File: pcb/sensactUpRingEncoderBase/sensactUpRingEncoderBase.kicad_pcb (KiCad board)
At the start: 2 copper layers, 70 x 70 mm, 59 parts, among them J3 BaseConnector, J5 ToBase, SW1 SW_Push, SW2 TERM ON OFF, SW3 RotaryEncoder, U27 TPS54202DDC, U4 AMS1117-3.3, U5 74AHCT1G125

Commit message: Layout Improvements, added VCML4040
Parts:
- SW1: footprint Button_Switch_THT:SW_PUSH_6mm_H4.3mm -> liebler_MECH:Button_12mm_ANCHOR_CENTER
- moved SW1 3.95 mm to (100.0, 100.0)
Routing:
- net SCL_EXT: track 31.1 -> 34.5 mm
- net SDA_EXT: track 33.7 -> 36.9 mm
- net Onewire: track 30.2 -> 32.8 mm
- net CANH: track 60.1 -> 62.6 mm
- net CANL: track 67.7 -> 70.2 mm
- net S: track 31.4 -> 33.5 mm
- net GND: vias 72 -> 127
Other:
- outline, holes or cut-outs redrawn

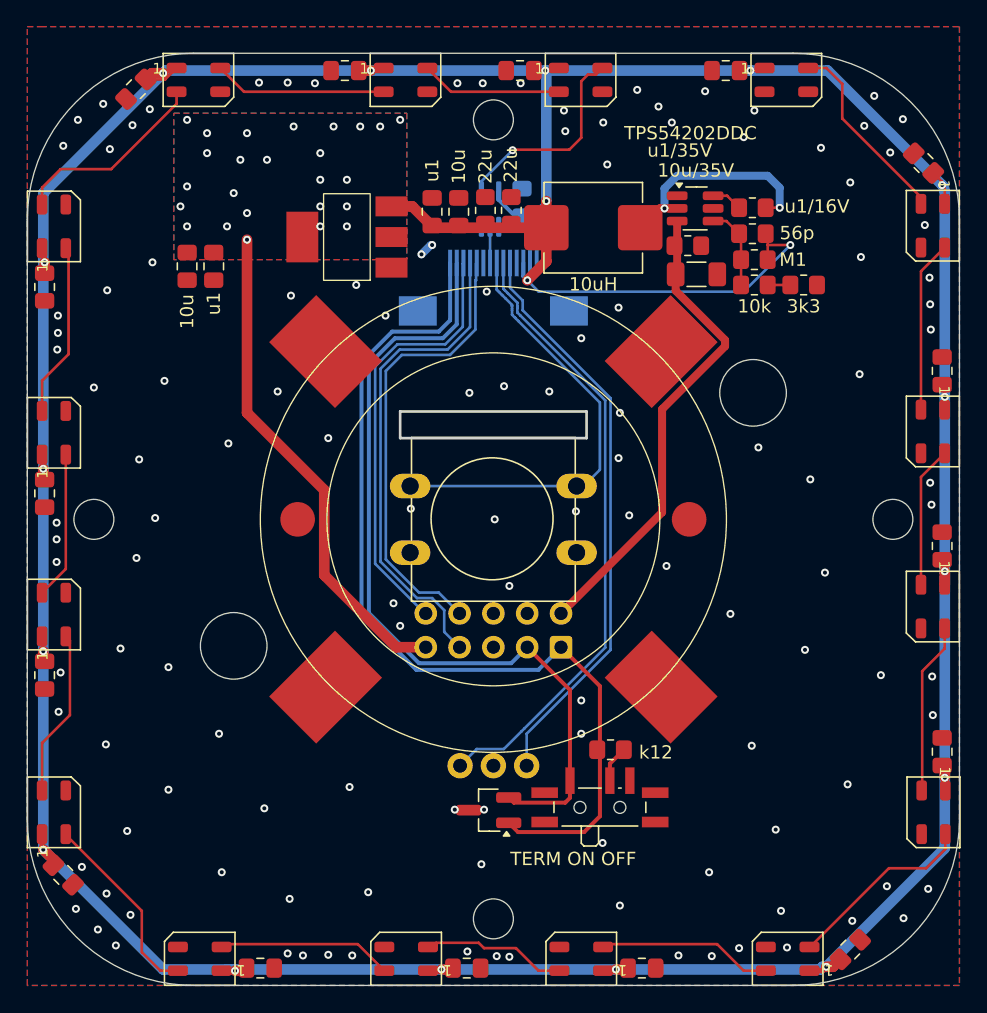
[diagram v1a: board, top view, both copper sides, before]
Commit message: Various updates in sensactRingEncoder
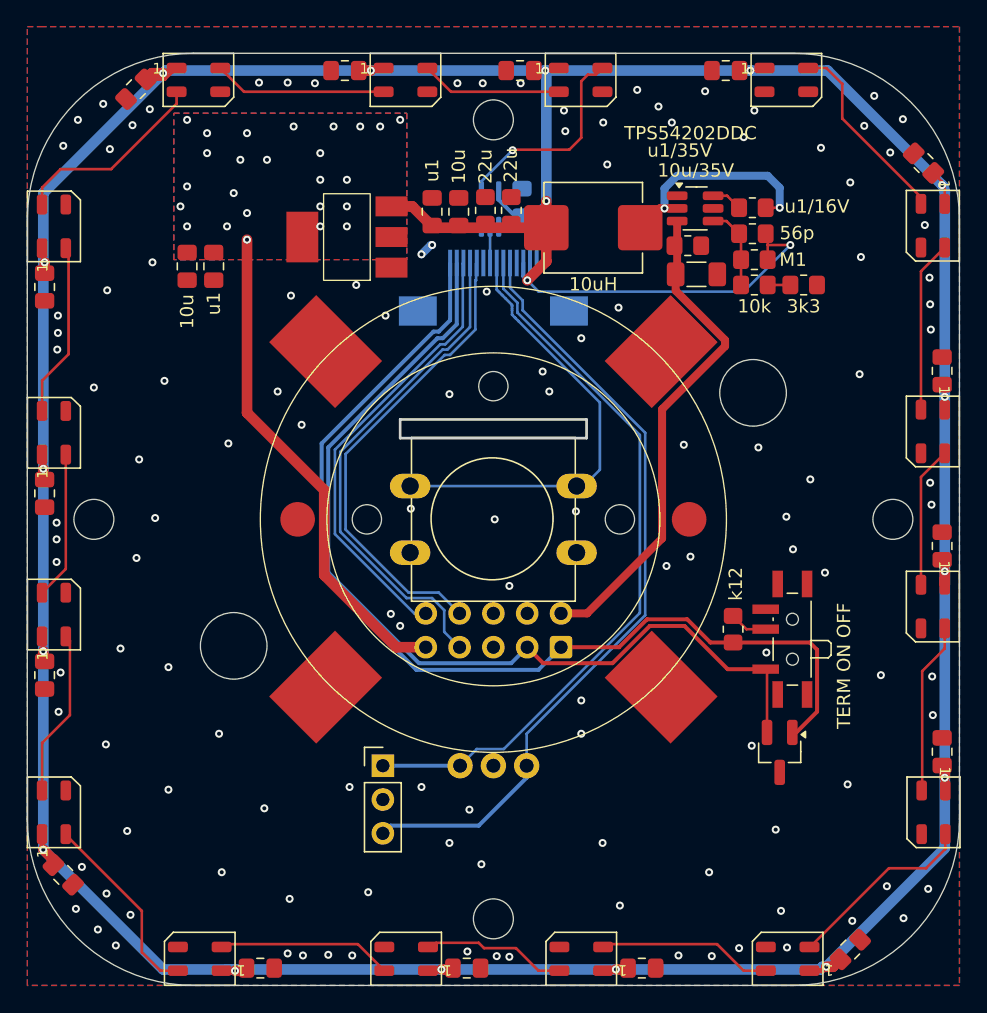
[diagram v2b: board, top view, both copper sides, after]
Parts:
- added H3: MountingHole, MountingHole:MountingHole_2.2mm_M2, F.Cu at (100.0, 90.0)
- added H4: MountingHole, MountingHole:MountingHole_2.2mm_M2, F.Cu at (90.5, 100.0)
- added H5: MountingHole, MountingHole:MountingHole_2.2mm_M2, F.Cu at (109.5, 100.0)
- added J1: ROT_EXT, Connector_PinHeader_2.54mm:PinHeader_1x03_P2.54mm_Vertical, F.Cu at (91.7, 118.5)
- moved D1 22.3 mm to (121.5, 117.5), turned to -90 degrees
- moved SW2 18.7 mm to (122.1, 109.0), turned to 90 degrees
- moved R1 12.9 mm to (118.0, 108.2), turned to 90 degrees
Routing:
- net A: track 43.5 -> 59.1 mm
- net CANH: track 62.6 -> 71.4 mm
- net B: track 46.6 -> 54.6 mm
- net CANL: track 70.2 -> 77.5 mm
- net +24V: track 39.7 -> 40.9 mm
- net Onewire: track 32.8 -> 33.9 mm
- net SDA_EXT: track 36.9 -> 37.9 mm
- net SCL_EXT: track 34.5 -> 35.5 mm
- net GND: vias 127 -> 128
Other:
- outline, holes or cut-outs redrawn

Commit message: sensactRingEncoder as ordered @ JLCPCB
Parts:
- added C48: 10u, Capacitor_SMD:C_0805_2012Metric_Pad1.18x1.45mm_HandSolder, F.Cu at (120.2, 101.3)
- added C53: u1, Capacitor_SMD:C_0805_2012Metric_Pad1.18x1.45mm_HandSolder, F.Cu at (122.2, 101.3)
- added C54: u1, Capacitor_SMD:C_0805_2012Metric_Pad1.18x1.45mm_HandSolder, F.Cu at (124.2, 101.3)
- added C55: 10u, Capacitor_SMD:C_0805_2012Metric_Pad1.18x1.45mm_HandSolder, F.Cu at (115.8, 117.6)
- added J7: PowerOutput, Connector_PinHeader_2.54mm:PinHeader_1x05_P2.54mm_Vertical, F.Cu at (77.3, 115.5)
- added JP1: Onewire2Out3, Jumper:SolderJumper-2_P1.3mm_Open_RoundedPad1.0x1.5mm, F.Cu at (92.8, 119.0)
- added JP2: Sda2Out4, Jumper:SolderJumper-2_P1.3mm_Open_RoundedPad1.0x1.5mm, F.Cu at (90.3, 119.0)
- added Q2: AO6800-HXY, Package_TO_SOT_SMD:SOT-23-6_Handsoldering, F.Cu at (76.7, 104.1)
- added Q3: AO6800-HXY, Package_TO_SOT_SMD:SOT-23-6_Handsoldering, F.Cu at (85.5, 118.5)
- added R55: 1k, Resistor_SMD:R_0805_2012Metric_Pad1.20x1.40mm_HandSolder, F.Cu at (76.7, 96.8)
- added R56: 1k, Resistor_SMD:R_0805_2012Metric_Pad1.20x1.40mm_HandSolder, F.Cu at (76.7, 94.9)
- added R57: 1k, Resistor_SMD:R_0805_2012Metric_Pad1.20x1.40mm_HandSolder, F.Cu at (92.5, 122.5)
- added R58: 1k, Resistor_SMD:R_0805_2012Metric_Pad1.20x1.40mm_HandSolder, F.Cu at (90.6, 122.5)
- added R61: M1, Resistor_SMD:R_0805_2012Metric_Pad1.20x1.40mm_HandSolder, F.Cu at (76.7, 100.7)
- added R62: M1, Resistor_SMD:R_0805_2012Metric_Pad1.20x1.40mm_HandSolder, F.Cu at (76.7, 98.8)
- added R63: M1, Resistor_SMD:R_0805_2012Metric_Pad1.20x1.40mm_HandSolder, F.Cu at (94.4, 122.5)
- added R64: M1, Resistor_SMD:R_0805_2012Metric_Pad1.20x1.40mm_HandSolder, F.Cu at (88.7, 122.5)
- added U7: AMS1117-12, liebler_SEMICONDUCTORS:SOT-223-3_TabPin2_HANDSOLDER, F.Cu at (121.6, 108.4)
- J1: footprint Connector_PinHeader_2.54mm:PinHeader_1x03_P2.54mm_Vertical -> liebler_CONN:PhoenixContact_MCV_1,5_3-G-3.5_1x03_P3.50mm_Vertical_smallerCourtyard; moved to B.Cu
- moved SW2 17.4 mm to (110.0, 121.5), turned to 0 degrees
- moved R1 12.6 mm to (109.6, 117.6), turned to 180 degrees
- moved J1 8.70 mm to (100.0, 121.1)
- moved D1 6.41 mm to (118.2, 123.0), turned to 0 degrees
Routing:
- net +12V: track 0.00 -> 53.0 mm, vias 0 -> 30
- net BaseIO1: track 2.72 -> 35.3 mm, vias 0 -> 1
- net BaseIO2: track 0.00 -> 28.9 mm, vias 0 -> 1
- net GND: track 1.09 -> 24.9 mm, vias 128 -> 243
- net Onewire: track 33.9 -> 50.0 mm
- net +24V: track 40.9 -> 54.4 mm
- net Net-(J7-Pin_2): track 0.00 -> 12.5 mm
- net Net-(Q3A-G): track 0.00 -> 12.4 mm
- net SDA_EXT: track 37.9 -> 50.2 mm
- net Net-(J7-Pin_1): track 0.00 -> 10.7 mm
- net A: track 59.1 -> 48.7 mm
- net CANL: track 77.5 -> 67.6 mm
- net Net-(Q2B-G): track 0.00 -> 9.32 mm
- net Net-(Q3B-G): track 0.00 -> 7.80 mm
- net Net-(Q2A-G): track 0.00 -> 6.72 mm
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- added copper zone on B.Cu, net +12V
- added copper zone on F.Cu, net +12V
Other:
- board text added: "12V"
- board text added: "BaseIO1"
- board text added: "BaseIO2"
- board text added: "Onewire"
- board text added: "SDA_EXT"
